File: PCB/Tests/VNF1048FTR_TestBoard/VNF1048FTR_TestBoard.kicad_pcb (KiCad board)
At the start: 2 copper layers, 29 parts, among them J1 Conn_01x10_Female, J2 Conn_01x02_Female, Q1 STL135N8F7AG, U1 VNF1048FTR

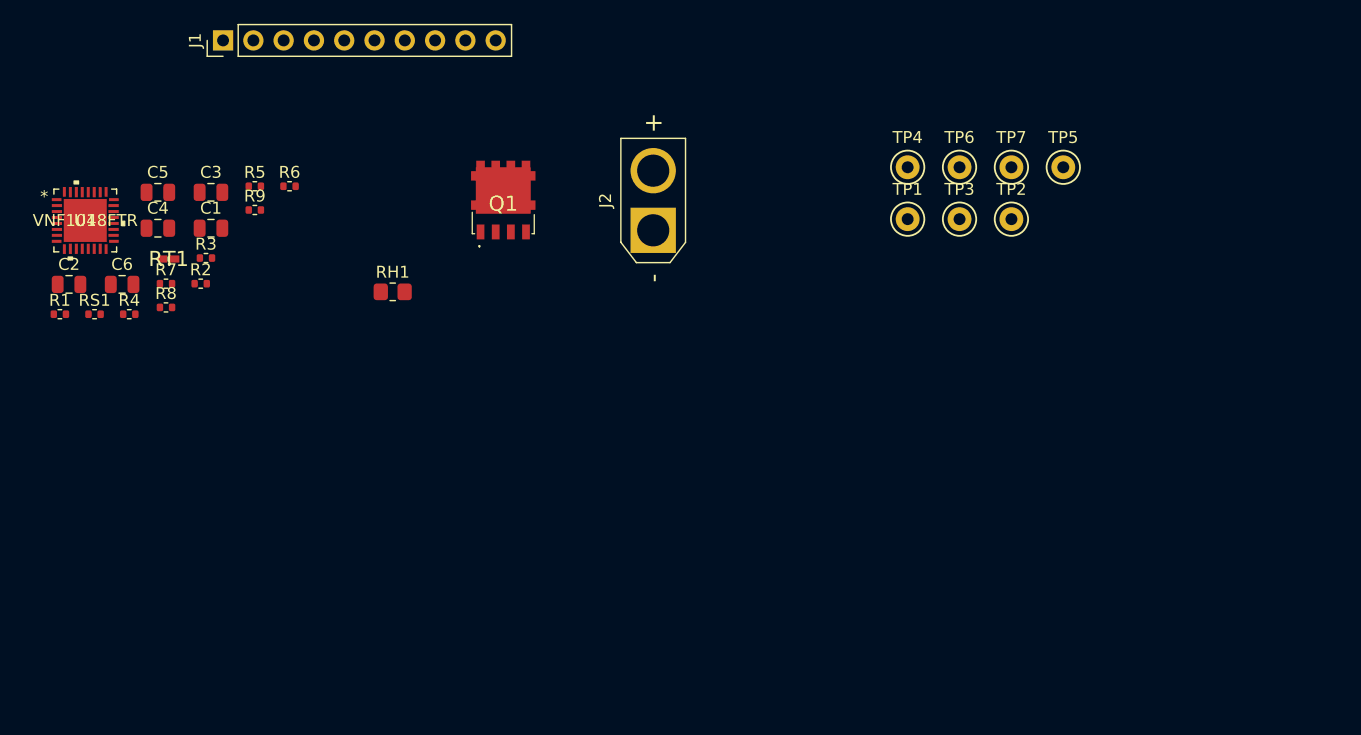
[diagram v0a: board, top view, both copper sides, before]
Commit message: VNF1048FTR TestBoard pcb layout change
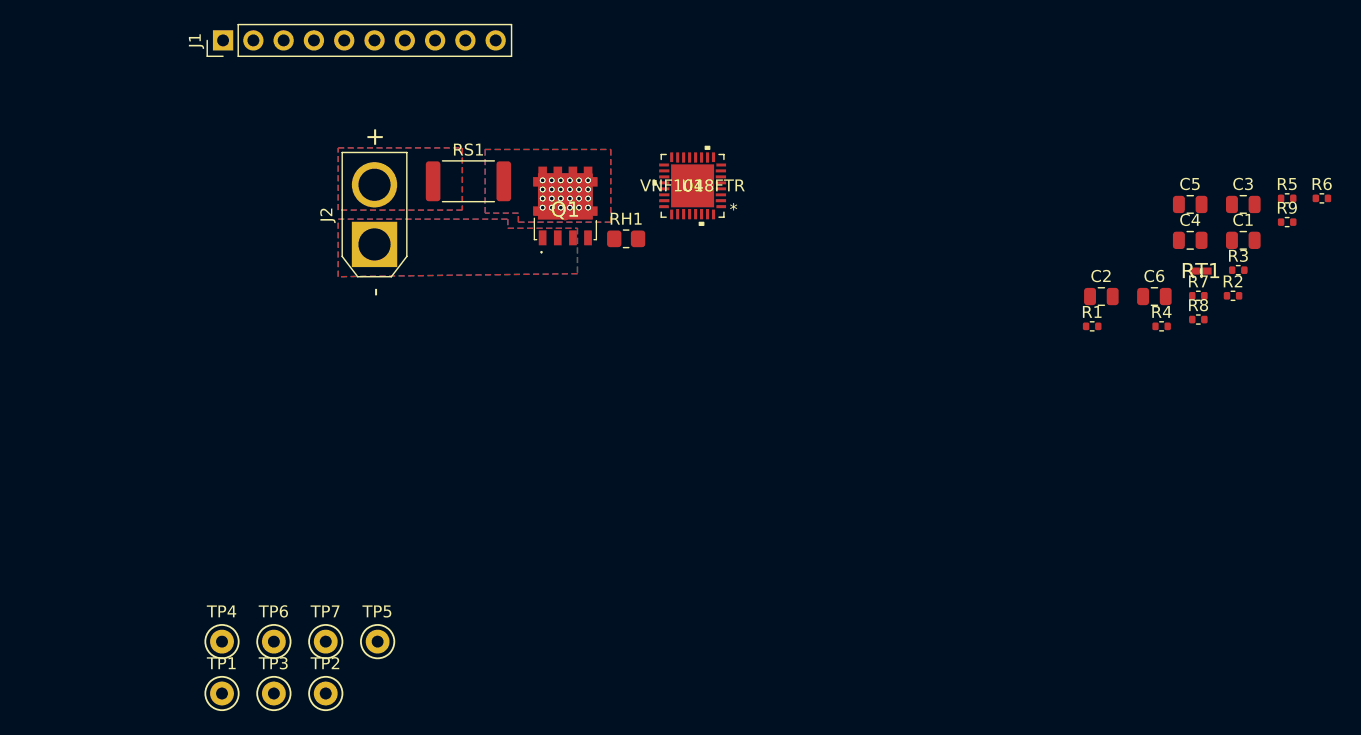
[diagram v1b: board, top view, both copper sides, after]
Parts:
- RS1: footprint Resistor_SMD:R_0402_1005Metric -> Resistor_SMD:R_2512_6332Metric
- moved RT1 86.6 mm to (148.8, 40.2)
- moved C4 86.6 mm to (147.9, 37.6)
- moved C5 86.6 mm to (147.9, 34.6)
- moved C6 86.6 mm to (144.9, 42.3)
- moved R1 86.6 mm to (139.7, 44.8)
- moved R2 86.6 mm to (151.5, 42.2)
- moved R3 86.6 mm to (151.9, 40.1)
- moved R5 86.6 mm to (156.0, 34.1)
- moved R9 86.6 mm to (156.0, 36.1)
- moved C1 86.6 mm to (152.3, 37.6)
- moved C2 86.6 mm to (140.4, 42.3)
- moved C3 86.6 mm to (152.3, 34.6)
- moved R4 86.6 mm to (145.5, 44.8)
- moved R6 86.6 mm to (158.9, 34.1)
- moved R7 86.6 mm to (148.6, 42.2)
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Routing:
- net (no net): vias 0 -> 24
- added copper zone on B.Cu, net +12V
- added copper zone on F.Cu, net +12V
- added copper zone on B.Cu, net /VNF1048FTR/MOS_IN
- added copper zone on F.Cu, net /VNF1048FTR/MOS_IN
- added copper zone on B.Cu, net MOS_OUTPUT12V
- added copper zone on F.Cu, net MOS_OUTPUT12V

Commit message: Modified test board + gerbers
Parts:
- removed TP1: TestPoint_Small, TestPoint:TestPoint_Keystone_5000-5004_Miniature
- added J3: Conn_01x01_Female, Connector_Wire:SolderWire-2sqmm_1x01_D2mm_OD3.9mm, F.Cu at (109.1, 58.4)
- added J4: Conn_01x02_Female, Connector_PinSocket_2.54mm:PinSocket_1x02_P2.54mm_Vertical, F.Cu at (127.5, 42.7)
- J1: value Conn_01x10_Female -> Conn_01x06_Female; footprint Connector_PinHeader_2.54mm:PinHeader_1x10_P2.54mm_Vertical -> Connector_PinSocket_2.54mm:PinSocket_1x06_P2.54mm_Vertical
- J2: value Conn_01x02_Female -> Conn_01x01_Female; footprint Connector_AMASS:AMASS_XT30U-M_1x02_P5.0mm_Vertical -> Connector_Wire:SolderWire-2sqmm_1x01_D2mm_OD3.9mm
- R2: moved to B.Cu
- RH1: footprint Resistor_SMD:R_0805_2012Metric_Pad1.20x1.40mm_HandSolder -> Resistor_THT:R_Axial_DIN0204_L3.6mm_D1.6mm_P2.54mm_Vertical
- moved TP4 66.0 mm to (121.5, 34.5)
- moved TP2 58.1 mm to (116.6, 34.5)
- moved TP3 57.7 mm to (114.3, 37.3)
- moved J2 57.0 mm to (132.7, 58.4), turned to 0 degrees
- moved TP5 52.0 mm to (119.1, 37.3)
- moved TP7 51.7 mm to (111.8, 34.5), turned to 90 degrees
- moved TP6 51.2 mm to (109.5, 37.3), turned to 90 degrees
- moved R6 45.1 mm to (114.3, 40.4), turned to 90 degrees
- moved J1 43.3 mm to (109.0, 30.7)
- moved C1 40.9 mm to (112.5, 46.7)
- moved R5 39.9 mm to (116.6, 40.4), turned to 90 degrees
- moved R9 39.7 mm to (119.4, 51.3), turned to 90 degrees
- moved RS1 38.5 mm to (116.0, 58.4)
- moved Q1 37.5 mm to (124.4, 58.5), turned to 90 degrees
- moved R7 36.9 mm to (111.8, 40.4), turned to 90 degrees
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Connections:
- net Net-(R9-Pad2) renamed /VNF1048FTR/HS_GATE
- J1 pad 3: /VNF1048FTR/SDO -> /VNF1048FTR/SCK
- J1 pad 4: /VNF1048FTR/SDI -> /VNF1048FTR/SDO
- J1 pad 5: /VNF1048FTR/SCK -> /VNF1048FTR/SDI
- R1 pad 1: Net-(R1-Pad1) -> /VNF1048FTR/DIAG
- R2 pad 1: Net-(R1-Pad1) -> /VNF1048FTR/DIAG
- R7 pad 1: Net-(R7-Pad1) -> /VNF1048FTR/HWLO
- TP6 pad 1: Net-(R1-Pad1) -> /VNF1048FTR/DIAG
- TP7 pad 1: Net-(R7-Pad1) -> /VNF1048FTR/HWLO
- U1 pad 10: Net-(R7-Pad1) -> /VNF1048FTR/HWLO
- U1 pad 6: Net-(R1-Pad1) -> /VNF1048FTR/DIAG
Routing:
- net +12V: track 0.42 -> 28.5 mm, vias 0 -> 3
- net /VNF1048FTR/DIAG: track 0.00 -> 20.8 mm, vias 0 -> 2
- net /VNF1048FTR/HWLO: track 0.00 -> 15.9 mm
- net MOS_OUTPUT12V: track 0.00 -> 14.3 mm
- net /VNF1048FTR/SCK: track 0.00 -> 14.2 mm
- net /VNF1048FTR/CSN: track 0.00 -> 14.2 mm
- net /VNF1048FTR/SDO: track 0.00 -> 13.4 mm
- net /VNF1048FTR/SDI: track 0.00 -> 13.2 mm
- net +3.3V: track 0.00 -> 12.5 mm, vias 0 -> 1
- net Net-(R8-Pad1): track 0.00 -> 10.0 mm, vias 0 -> 2
- net GND: track 0.00 -> 8.77 mm, vias 0 -> 4
- net /VNF1048FTR/MOS_IN: track 0.48 -> 8.99 mm
- net /VNF1048FTR/HS_GATE: track 0.00 -> 6.60 mm
- net Net-(C3-Pad1): track 0.00 -> 5.94 mm
- net Net-(C2-Pad2): track 0.00 -> 4.97 mm
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- added copper zone on B.Cu, net GND
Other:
- board outline added: 33.2 x 35.8 mm
- board text added: "3.3V"
- board text added: "CSN"
- board text added: "EVAL by K.Pergol"
- board text added: "GND"
- board text added: "SCK"
- board text added: "SDI"
- board text added: "SDO"
